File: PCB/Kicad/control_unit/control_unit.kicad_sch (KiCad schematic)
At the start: 0 parts

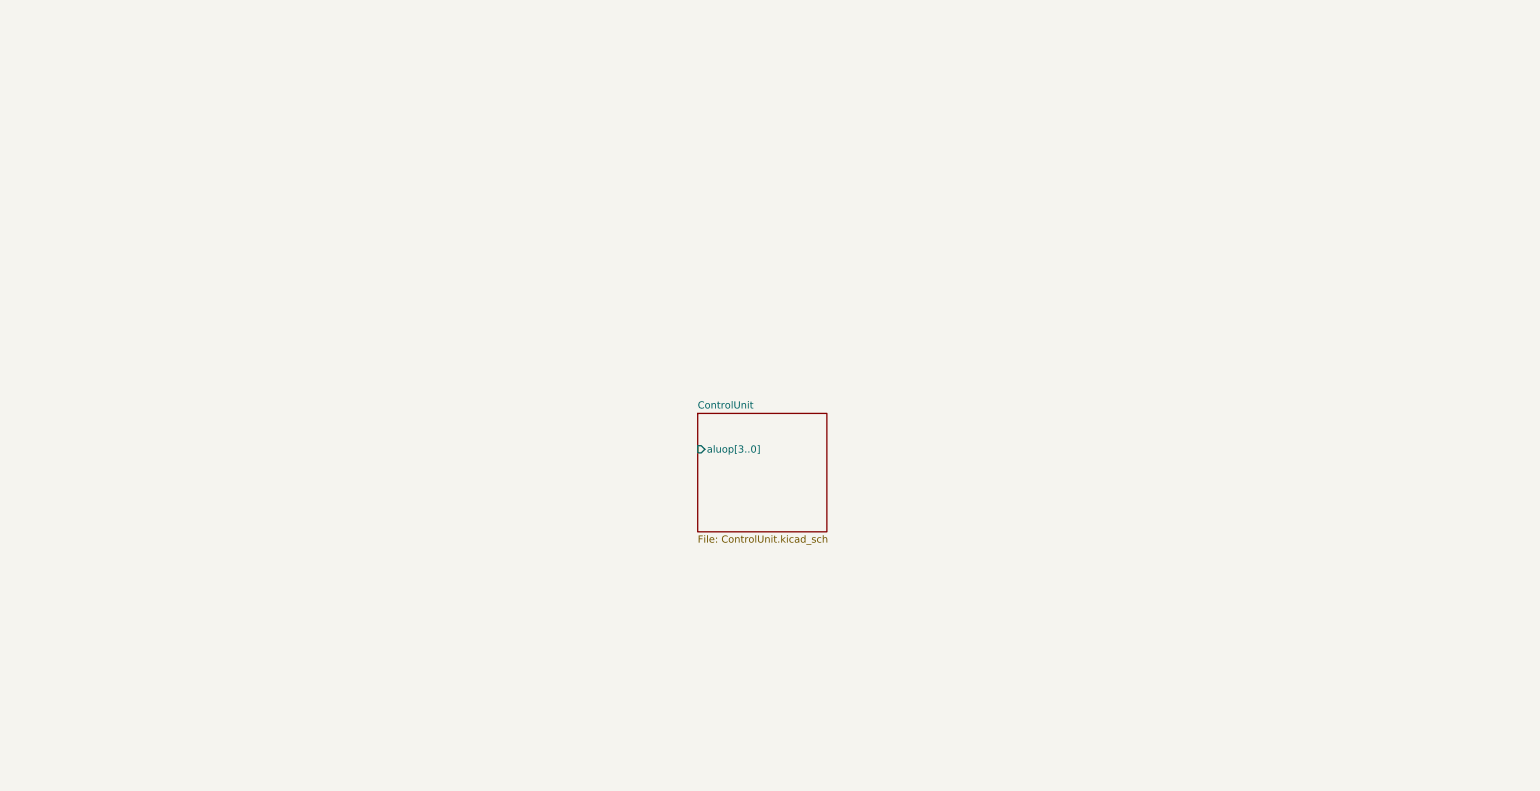
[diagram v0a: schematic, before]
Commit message: control unit schematic
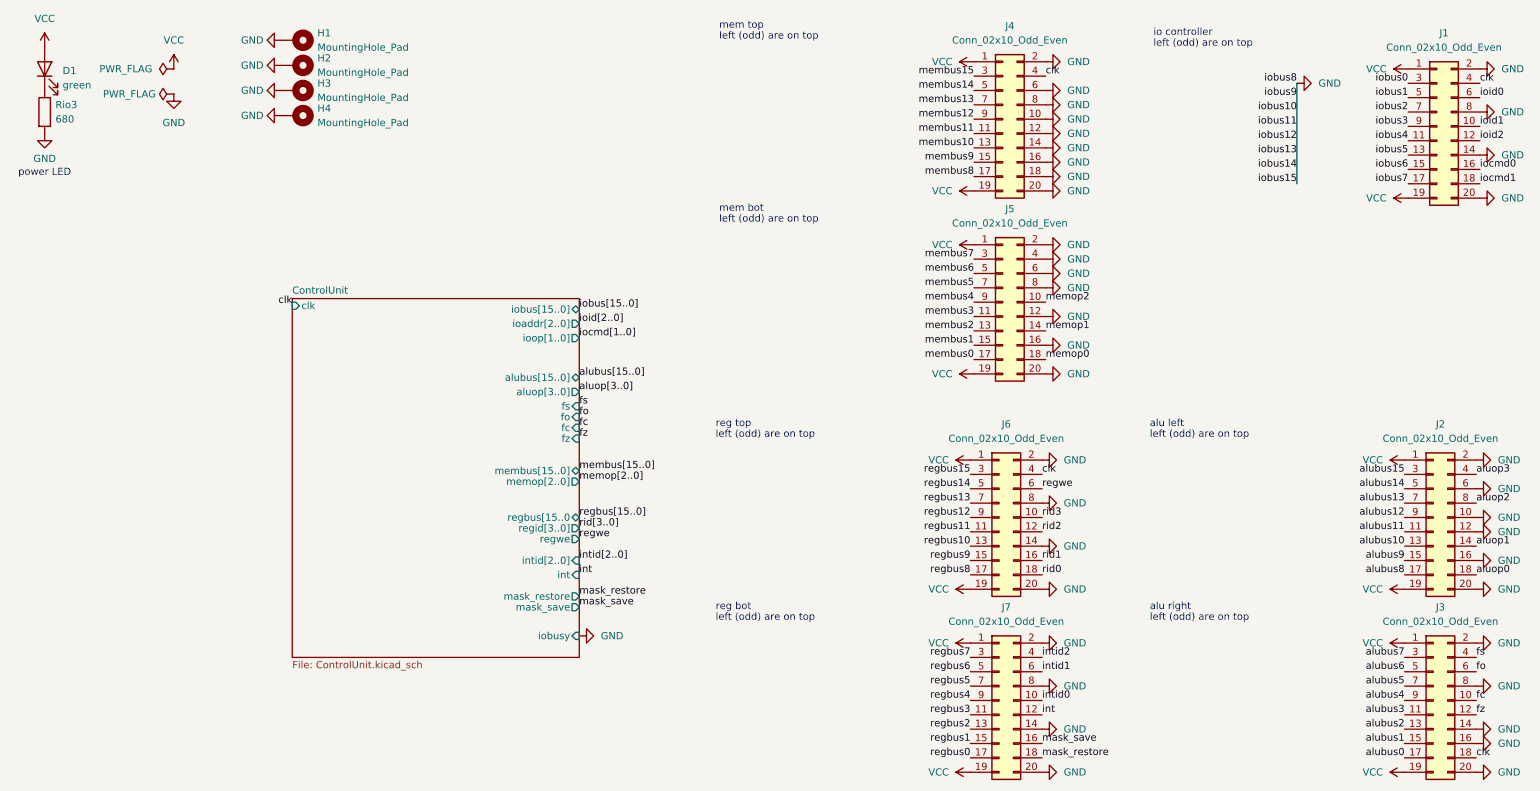
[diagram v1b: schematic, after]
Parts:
- added D1: green, Diode_SMD:D_0603_1608Metric, symbol Device:LED
- added H1, H2, H3, H4: MountingHole_Pad, MountingHole:MountingHole_2.2mm_M2_DIN965_Pad, symbol Mechanical:MountingHole_Pad
- added J1, J2, J3, J4, J5, J6, J7: Conn_02x10_Odd_Even, Connector_PinHeader_2.54mm:PinHeader_2x10_P2.54mm_Horizontal, symbol Connector_Generic:Conn_02x10_Odd_Even
- added Rio3: 680, Resistor_SMD:R_0402_1005Metric, symbol Device:R
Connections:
- new net: D1.1 (K), Rio3.1
- new net GND: H1.1, H2.1, H3.1, H4.1, J1.14 (Pin_14), J1.2 (Pin_2), J1.20 (Pin_20), J1.8 (Pin_8), J2.10 (Pin_10), J2.12 (Pin_12), J2.16 (Pin_16), J2.2 (Pin_2), J2.20 (Pin_20), J2.6 (Pin_6), J3.14 (Pin_14), J3.16 (Pin_16), J3.2 (Pin_2), J3.20 (Pin_20), J3.8 (Pin_8), J4.10 (Pin_10), J4.12 (Pin_12), J4.14 (Pin_14), J4.16 (Pin_16), J4.18 (Pin_18), J4.2 (Pin_2), J4.20 (Pin_20), J4.6 (Pin_6), J4.8 (Pin_8), J5.12 (Pin_12), J5.16 (Pin_16), J5.2 (Pin_2), J5.20 (Pin_20), J5.4 (Pin_4), J5.6 (Pin_6), J5.8 (Pin_8), J6.14 (Pin_14), J6.2 (Pin_2), J6.20 (Pin_20), J6.8 (Pin_8), J7.14 (Pin_14), J7.2 (Pin_2), J7.20 (Pin_20), J7.8 (Pin_8), Rio3.2
- new net VCC: D1.2 (A), J1.1 (Pin_1), J1.19 (Pin_19), J2.1 (Pin_1), J2.19 (Pin_19), J3.1 (Pin_1), J3.19 (Pin_19), J4.1 (Pin_1), J4.19 (Pin_19), J5.1 (Pin_1), J5.19 (Pin_19), J6.1 (Pin_1), J6.19 (Pin_19), J7.1 (Pin_1), J7.19 (Pin_19)
- new net alubus0: J3.17 (Pin_17)
- new net alubus1: J3.15 (Pin_15)
- new net alubus10: J2.13 (Pin_13)
- new net alubus11: J2.11 (Pin_11)
- new net alubus12: J2.9 (Pin_9)
- new net alubus13: J2.7 (Pin_7)
- new net alubus14: J2.5 (Pin_5)
- new net alubus15: J2.3 (Pin_3)
- new net alubus2: J3.13 (Pin_13)
- new net alubus3: J3.11 (Pin_11)
- new net alubus4: J3.9 (Pin_9)
- new net alubus5: J3.7 (Pin_7)
- new net alubus6: J3.5 (Pin_5)
- new net alubus7: J3.3 (Pin_3)
- new net alubus8: J2.17 (Pin_17)
- new net alubus9: J2.15 (Pin_15)
- new net aluop0: J2.18 (Pin_18)
- new net aluop1: J2.14 (Pin_14)
- new net aluop2: J2.8 (Pin_8)
- new net aluop3: J2.4 (Pin_4)
- new net clk: J1.4 (Pin_4), J3.18 (Pin_18), J4.4 (Pin_4), J6.4 (Pin_4)
- new net fc: J3.10 (Pin_10)
- new net fo: J3.6 (Pin_6)
- new net fs: J3.4 (Pin_4)
- new net fz: J3.12 (Pin_12)
- new net int: J7.12 (Pin_12)
- new net intid0: J7.10 (Pin_10)
- new net intid1: J7.6 (Pin_6)
- new net intid2: J7.4 (Pin_4)
- new net iobus0: J1.3 (Pin_3)
- new net iobus1: J1.5 (Pin_5)
- new net iobus2: J1.7 (Pin_7)
- new net iobus3: J1.9 (Pin_9)
- new net iobus4: J1.11 (Pin_11)
- new net iobus5: J1.13 (Pin_13)
- new net iobus6: J1.15 (Pin_15)
- new net iobus7: J1.17 (Pin_17)
- new net iocmd0: J1.16 (Pin_16)
- new net iocmd1: J1.18 (Pin_18)
- new net ioid0: J1.6 (Pin_6)
- new net ioid1: J1.10 (Pin_10)
- new net ioid2: J1.12 (Pin_12)
- new net mask_restore: J7.18 (Pin_18)
- new net mask_save: J7.16 (Pin_16)
- new net membus0: J5.17 (Pin_17)
- new net membus1: J5.15 (Pin_15)
- new net membus10: J4.13 (Pin_13)
- new net membus11: J4.11 (Pin_11)
- new net membus12: J4.9 (Pin_9)
- new net membus13: J4.7 (Pin_7)
- new net membus14: J4.5 (Pin_5)
- new net membus15: J4.3 (Pin_3)
- new net membus2: J5.13 (Pin_13)
- new net membus3: J5.11 (Pin_11)
- new net membus4: J5.9 (Pin_9)
- new net membus5: J5.7 (Pin_7)
- new net membus6: J5.5 (Pin_5)
- new net membus7: J5.3 (Pin_3)
- new net membus8: J4.17 (Pin_17)
- new net membus9: J4.15 (Pin_15)
- new net memop0: J5.18 (Pin_18)
- new net memop1: J5.14 (Pin_14)
- new net memop2: J5.10 (Pin_10)
- new net regbus0: J7.17 (Pin_17)
- new net regbus1: J7.15 (Pin_15)
- new net regbus10: J6.13 (Pin_13)
- new net regbus11: J6.11 (Pin_11)
- new net regbus12: J6.9 (Pin_9)
- new net regbus13: J6.7 (Pin_7)
- new net regbus14: J6.5 (Pin_5)
- new net regbus15: J6.3 (Pin_3)
- new net regbus2: J7.13 (Pin_13)
- new net regbus3: J7.11 (Pin_11)
- new net regbus4: J7.9 (Pin_9)
- new net regbus5: J7.7 (Pin_7)
- new net regbus6: J7.5 (Pin_5)
- new net regbus7: J7.3 (Pin_3)
- new net regbus8: J6.17 (Pin_17)
- new net regbus9: J6.15 (Pin_15)
- new net regwe: J6.6 (Pin_6)
- new net rid0: J6.18 (Pin_18)
- new net rid1: J6.16 (Pin_16)
- new net rid2: J6.12 (Pin_12)
- new net rid3: J6.10 (Pin_10)
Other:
- sheet ControlUnit ports: added alubus[15..0], clk, fc, fo, fs, fz, int, intid[2..0], ioaddr[2..0], iobus[15..0], iobusy, ioop[1..0], mask_restore, mask_save, membus[15..0], memop[2..0], regbus[15..0, regid[3..0], regwe; removed none
- note added: "alu left"
- note added: "alu right"
- note added: "io controller"
- note added: "left (odd) are on top"
- note added: "mem bot"
- note added: "mem top"
- note added: "power LED"
- note added: "reg bot"
- note added: "reg top"

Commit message: control unit update
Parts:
- added J8: in, mALUch_lib:PinHeader_2x10_P2.54mm_Horizontal, symbol Connector_Generic:Conn_02x10_Odd_Even
- D1: footprint Diode_SMD:D_0603_1608Metric -> LED_SMD:LED_0603_1608Metric
- H1, H2, H3, H4: now not fitted
- J1, J2, J3, J4, J5, J6, J7: value Conn_02x10_Odd_Even -> in; footprint Connector_PinHeader_2.54mm:PinHeader_2x10_P2.54mm_Horizontal -> mALUch_lib:PinHeader_2x10_P2.54mm_Horizontal
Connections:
- net GND: now also J4.4 (Pin_4), J5.10 (Pin_10), J5.14 (Pin_14), J5.18 (Pin_18), J8.1 (Pin_1), J8.10 (Pin_10), J8.12 (Pin_12), J8.14 (Pin_14), J8.16 (Pin_16), J8.18 (Pin_18), J8.2 (Pin_2), J8.20 (Pin_20), J8.4 (Pin_4), J8.6 (Pin_6), J8.7 (Pin_7), J8.8 (Pin_8); no longer J4.18 (Pin_18), J5.12 (Pin_12), J5.4 (Pin_4), J5.8 (Pin_8)
- net VCC: now also J8.11 (Pin_11), J8.13 (Pin_13), J8.15 (Pin_15), J8.17 (Pin_17), J8.19 (Pin_19), J8.9 (Pin_9)
- net clk: now also J4.18 (Pin_18), J8.3 (Pin_3), J8.5 (Pin_5); no longer J4.4 (Pin_4)
- net membus0: now also J5.3 (Pin_3); no longer J5.17 (Pin_17)
- net membus1: now also J5.5 (Pin_5); no longer J5.15 (Pin_15)
- net membus10: now also J4.7 (Pin_7); no longer J4.13 (Pin_13)
- net membus11: now also J4.9 (Pin_9); no longer J4.11 (Pin_11)
- net membus12: now also J4.11 (Pin_11); no longer J4.9 (Pin_9)
- net membus13: now also J4.13 (Pin_13); no longer J4.7 (Pin_7)
- net membus14: now also J4.15 (Pin_15); no longer J4.5 (Pin_5)
- net membus15: now also J4.17 (Pin_17); no longer J4.3 (Pin_3)
- net membus2: now also J5.7 (Pin_7); no longer J5.13 (Pin_13)
- net membus3: now also J5.9 (Pin_9); no longer J5.11 (Pin_11)
- net membus4: now also J5.11 (Pin_11); no longer J5.9 (Pin_9)
- net membus5: now also J5.13 (Pin_13); no longer J5.7 (Pin_7)
- net membus6: now also J5.15 (Pin_15); no longer J5.5 (Pin_5)
- net membus7: now also J5.17 (Pin_17); no longer J5.3 (Pin_3)
- net membus8: now also J4.3 (Pin_3); no longer J4.17 (Pin_17)
- net membus9: now also J4.5 (Pin_5); no longer J4.15 (Pin_15)
- net memop0: now also J5.4 (Pin_4); no longer J5.18 (Pin_18)
- net memop1: now also J5.8 (Pin_8); no longer J5.14 (Pin_14)
- net memop2: now also J5.12 (Pin_12); no longer J5.10 (Pin_10)
